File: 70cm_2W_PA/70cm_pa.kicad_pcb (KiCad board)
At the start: 2 copper layers, 48.3 x 48.3 mm, 48 parts, among them J3 Conn_01x02, U1 M68710L, U2 MIC5205YM5, U3 SN74LV1T08

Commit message: M68710L: everything is connected again
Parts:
- removed C11: 100n, Capacitor_SMD:C_0805_2012Metric
- R15: value ~ -> 100k
- moved C7 6.87 mm to (57.8, 59.7), turned to 90 degrees
- moved C9 5.12 mm to (45.1, 55.9), turned to 270 degrees
- moved R19 3.86 mm to (41.3, 58.4)
- moved R15 3.42 mm to (45.7, 50.8), turned to 180 degrees
- moved R20 3.18 mm to (41.9, 60.3), turned to 180 degrees
- moved R16 1.80 mm to (41.9, 52.1)
- moved R18 1.42 mm to (45.7, 52.7), turned to 180 degrees
- moved U3 1.42 mm to (41.9, 55.2)
- moved C1 0.63 mm to (49.5, 50.8)
- moved R11 0.63 mm to (49.5, 52.7), turned to 180 degrees
- moved R17 0.63 mm to (43.8, 60.3), turned to 180 degrees
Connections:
- C9 pad 2: Net-(C9-Pad2) -> GND
- R10 pad 1: VCC -> /REG_OUT
- R11 pad 1: Net-(C9-Pad2) -> /REG_OUT
- R11 pad 2: GND -> VCC
- R9 pad 1: VCC -> /REG_OUT
- U2 pad 5: VCC -> /REG_OUT
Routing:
- net VCC: track 4.32 -> 17.8 mm
- net GND: track 4.93 -> 18.1 mm, vias 354 -> 365
- net /V_supply: track 13.0 -> 23.1 mm
- net /NTC2: track 0.00 -> 9.64 mm
- net Net-(R19-Pad1): track 0.00 -> 7.52 mm
- net /V_in: track 2.51 -> 9.48 mm
- net Net-(R15-Pad1): track 0.00 -> 6.91 mm
- net /REG_OUT: track 0.00 -> 6.57 mm
- net /PA_VGG: track 3.27 -> 6.03 mm
- net /EN: track 6.54 -> 8.02 mm

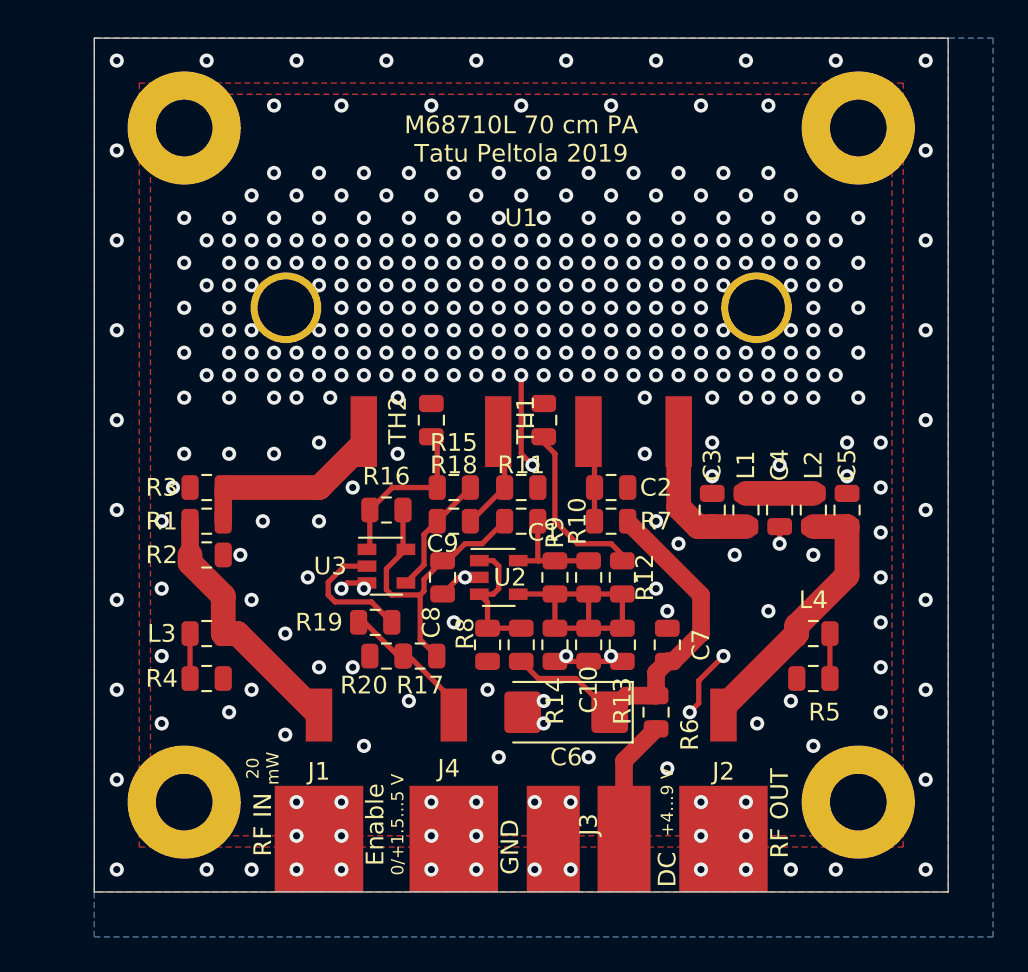
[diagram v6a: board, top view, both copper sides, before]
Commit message: M68710L: Add more filtering and improve layout
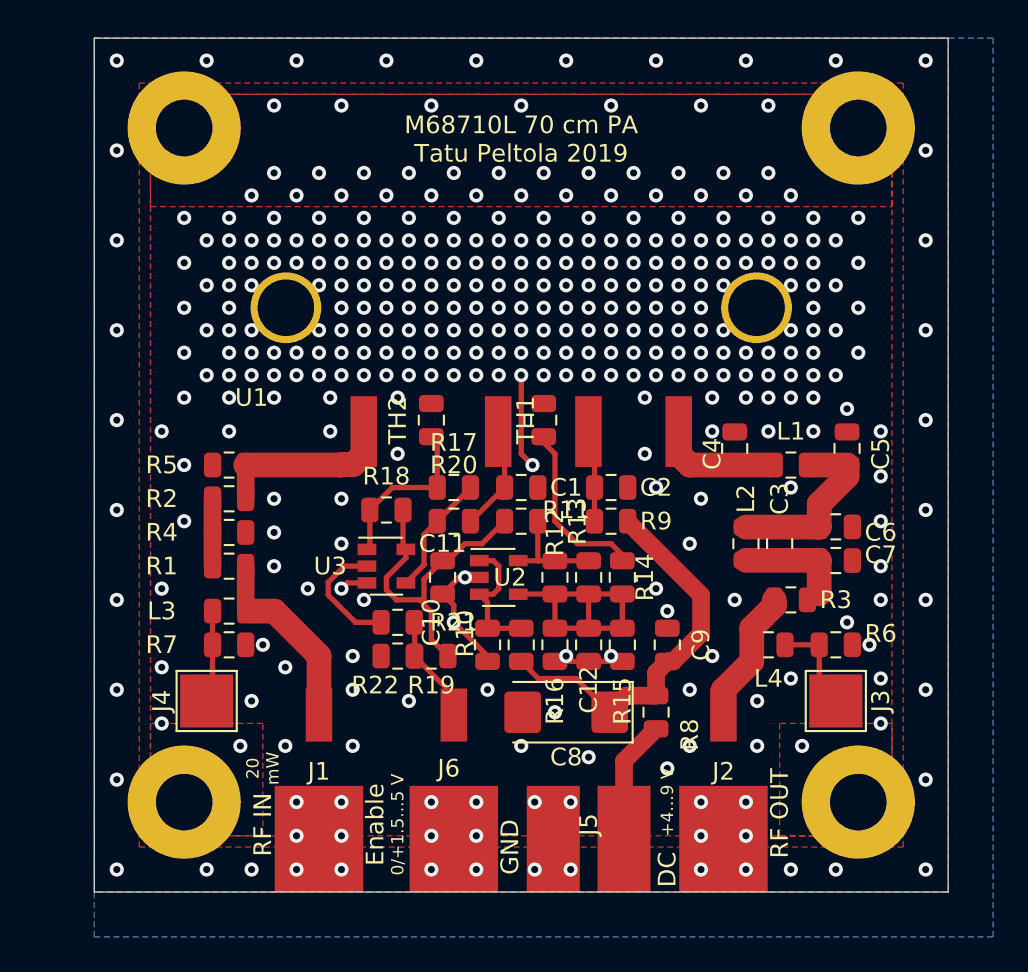
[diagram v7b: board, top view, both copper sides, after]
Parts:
- removed the C5 at (67.9, 52.1)
- removed the R4 at (31.8, 61.6)
- added C3: 2p2, Capacitor_SMD:C_0805_2012Metric, F.Cu at (64.1, 54.0)
- added C6: 10p, Capacitor_SMD:C_0805_2012Metric, F.Cu at (67.3, 53.0)
- added C7: 10p, Capacitor_SMD:C_0805_2012Metric, F.Cu at (67.3, 54.9)
- added J3: ~, TestPoint:TestPoint_Pad_3.0x3.0mm, F.Cu at (67.3, 62.9)
- added J4: ~, TestPoint:TestPoint_Pad_3.0x3.0mm, F.Cu at (31.8, 62.9)
- added R1: 0, Resistor_SMD:R_0805_2012Metric, F.Cu at (33.0, 55.2)
- added R3: 0, Resistor_SMD:R_0805_2012Metric, F.Cu at (64.8, 57.1)
- added R7: 0, Resistor_SMD:R_0805_2012Metric, F.Cu at (33.0, 59.7)
- C4: renamed from C3; value TBD -> ~
- C5: renamed from C4; value TBD -> ~
- L1: value TBD -> 0R
- L2: value TBD -> 12n
- moved C5 5.16 mm to (67.9, 48.6), turned to 90 degrees
- moved L2 4.26 mm to (62.2, 54.0)
- moved C4 3.70 mm to (61.6, 48.6)
- moved L1 3.59 mm to (64.8, 49.5), turned to 0 degrees
- moved L4 2.62 mm to (63.5, 59.7)
- moved R6 2.29 mm to (67.3, 59.7), turned to 0 degrees
- moved L3 1.80 mm to (33.0, 57.8)
- moved R2 1.80 mm to (33.0, 51.4)
- moved R4 1.80 mm to (33.0, 53.3)
- moved R5 1.80 mm to (33.0, 49.5)
- moved R21 1.27 mm to (42.5, 58.4), turned to 0 degrees
- moved R19 0.64 mm to (44.5, 60.3)
- moved R22 0.64 mm to (42.5, 60.3)
- renumbered C8 to C10, C9 to C11, C10 to C12, C6 to C8, C7 to C9, J3 to J5, J4 to J6, R8 to R10, R9 to R12, R10 to R13, R12 to R14, R13 to R15, R14 to R16, R15 to R17, R16 to R18, R17 to R19, R1 to R2, R18 to R20, R19 to R21, R20 to R22, R2 to R4, R3 to R5, R5 to R6, R6 to R8, R7 to R9
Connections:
- net Net-(L4-Pad2) renamed /BiasT_out
- L2 pad 2: /RF_out -> Net-(C3-Pad2)
- L3 pad 2: Net-(L3-Pad2) -> /BiasT_in
- R2 pad 2: /RF_in -> Net-(R1-Pad2)
- R4 pad 1: /RF_in -> Net-(R1-Pad2)
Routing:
- net /RF_out: track 15.5 -> 7.70 mm
- net Net-(C3-Pad1): track 3.81 -> 10.5 mm
- net Net-(C3-Pad2): track 0.00 -> 6.04 mm
- net /BiasT_in: track 0.00 -> 5.22 mm
- net Net-(R1-Pad2): track 0.00 -> 3.81 mm
- net /RF_in: track 14.4 -> 10.7 mm
- net /BiasT_out: track 2.54 -> 5.50 mm
- net Net-(L3-Pad2): track 2.54 -> 0.00 mm
- net /EN: track 8.02 -> 6.18 mm
- net /PA_out: track 8.53 -> 6.93 mm
- net Net-(R21-Pad1): track 7.52 -> 6.91 mm
- net VCC: track 17.8 -> 18.3 mm
- net GND: vias 365 -> 364

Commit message: M68710L: Layout cleanup
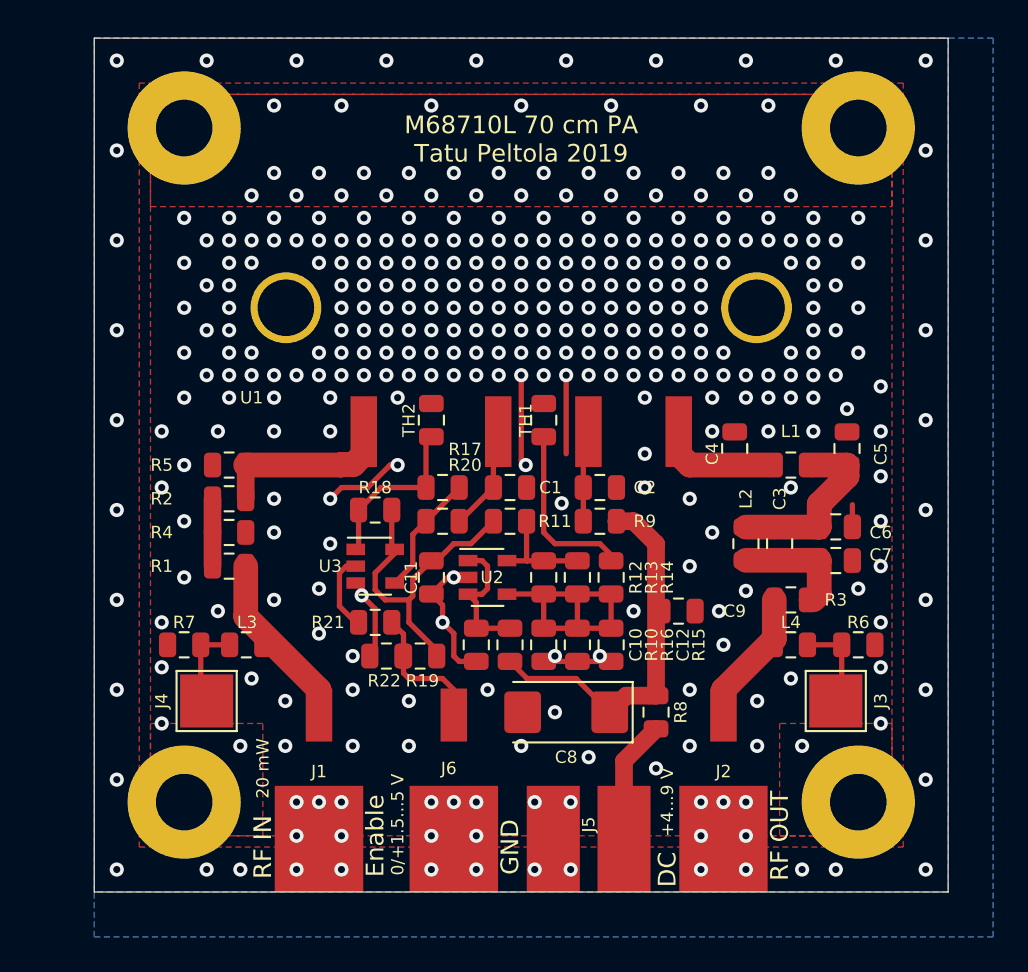
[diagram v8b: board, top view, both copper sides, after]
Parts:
- moved R7 2.54 mm to (30.5, 59.7), turned to 180 degrees
- moved L3 2.14 mm to (34.0, 59.7)
- moved C9 2.01 mm to (58.4, 57.8), turned to 0 degrees
- moved R21 1.27 mm to (41.3, 58.4)
- moved L4 1.27 mm to (64.8, 59.7)
- moved R6 1.27 mm to (68.6, 59.7)
- moved C12 0.64 mm to (52.7, 59.7)
- moved R12 0.64 mm to (50.8, 55.9)
- moved R13 0.64 mm to (52.7, 55.9)
- moved R16 0.64 mm to (50.8, 59.7)
- moved R19 0.64 mm to (43.8, 60.3)
- moved R22 0.64 mm to (41.9, 60.3)
- moved C1 0.63 mm to (48.9, 50.8)
- moved C10 0.63 mm to (47.0, 59.7)
- moved C11 0.63 mm to (44.5, 55.9)
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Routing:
- net GND: track 18.1 -> 32.2 mm, vias 364 -> 357
- net Net-(R21-Pad1): track 6.91 -> 4.42 mm
- net /EN: track 6.18 -> 7.81 mm
- net /V_supply: track 23.1 -> 22.3 mm
- net Net-(C3-Pad2): track 6.04 -> 6.84 mm
- net /RF_in: track 10.7 -> 10.1 mm
